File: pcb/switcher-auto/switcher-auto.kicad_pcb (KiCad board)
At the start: 4 copper layers, 234.9 x 89 mm, 120 parts, among them J1 MD-90SM, J2 Conn_02x22_Top_Bottom, J201 MD-90SM, J202 MD-90SM, J203 MD-90SM, J204 MD-90SM, J205 MD-90SM, J206 Conn_02x22_Top_Bottom, J3 Conn_02x22_Top_Bottom, J4 Conn_02x22_Top_Bottom, U1 CD74HC4067SM, U11 THS7374, U2 CD74HC4067SM, U3 CD74HC4067SM, U4 CD74HC4067SM, U5 MUX506IPWR, U6 MUX506IPWR, U7 CD74HC4067SM, U8 LM2776

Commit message: Routing checkpoint
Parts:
- removed C8: 1u, Capacitor_SMD:C_0805_2012Metric_Pad1.18x1.45mm_HandSolder
- C12: value 0.1u -> 22uF
- moved C9 1.44 mm to (58.0, 98.1), turned to 0 degrees
- moved C10 1.20 mm to (58.0, 94.9), turned to 180 degrees
- moved C13 0.33 mm to (61.6, 81.5)
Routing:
- net -5V: track 32.3 -> 59.3 mm, vias 0 -> 3
- net GND: track 33.8 -> 53.9 mm, vias 31 -> 33
- net VCC: track 43.7 -> 28.7 mm
- net /9_BVID: track 41.3 -> 39.1 mm
- net /5_BVID: track 47.1 -> 45.0 mm
- net /6_BVID: track 50.2 -> 48.2 mm
- net /7_BVID: track 53.4 -> 51.4 mm
- net /10_RAUD: track 96.4 -> 95.2 mm
- net /8_BVID: track 40.8 -> 39.6 mm
- net /11_RAUD: track 94.9 -> 94.0 mm
- net /12_RAUD: track 93.6 -> 92.8 mm
- net /6_RVID: track 64.3 -> 63.6 mm
- net /9_RVID: track 81.6 -> 81.0 mm
- net /7_RVID: track 66.7 -> 66.1 mm
- net /8_RVID: track 78.2 -> 77.6 mm
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- added copper zone on B.Cu, net GND
- added copper zone on In1.Cu, net GND
- added copper zone on In2.Cu, net VCC
- removed copper zone on In2.Cu, net GND
- removed copper zone on B.Cu, net VCC
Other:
- board text removed: "Note pin 1"

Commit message: Rev3
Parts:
- C10, C9: value 2.2uF -> 1uF
- J2: value Conn_02x22_Top_Bottom -> Inputs 0-4
- J3: value Conn_02x22_Top_Bottom -> Inputs 5-9
- J4: value Conn_02x22_Top_Bottom -> Inputs 10-14
- moved C14 0.84 mm to (66.1, 96.1), turned to -90 degrees
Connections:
- C14 pad 1: Net-(U8-C1+) -> Net-(U8-C1-)
- C14 pad 2: Net-(U8-C1-) -> Net-(U8-C1+)
- U5 pad 18: GND -> VCC
- U6 pad 18: GND -> VCC
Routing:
- net VCC: track 28.7 -> 31.8 mm, vias 12 -> 14
- net GND: track 53.9 -> 51.2 mm, vias 33 -> 31
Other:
- board text added: "${COMPANY}"
- board text added: "${TITLE} rev${REVISION}"
- board text added: "USB"

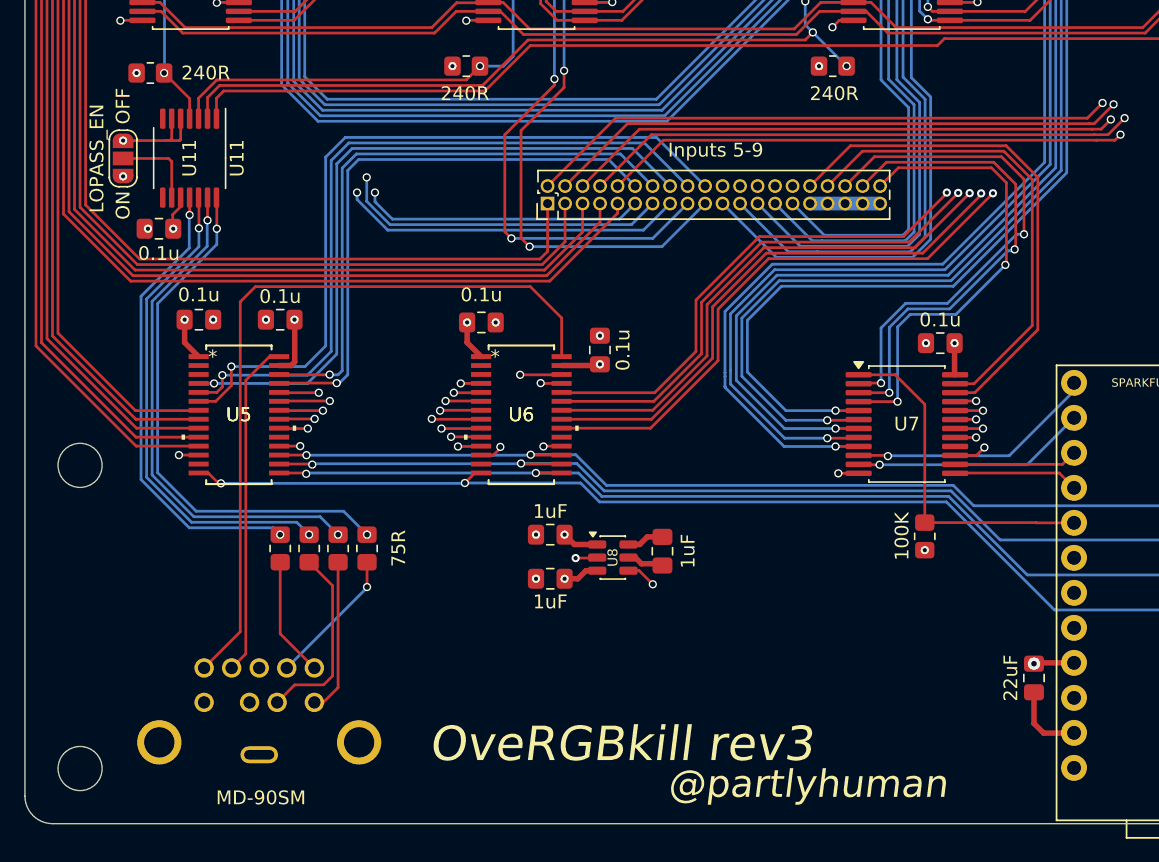
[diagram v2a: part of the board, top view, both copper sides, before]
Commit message: Switcher should run off 5V / RAW pin
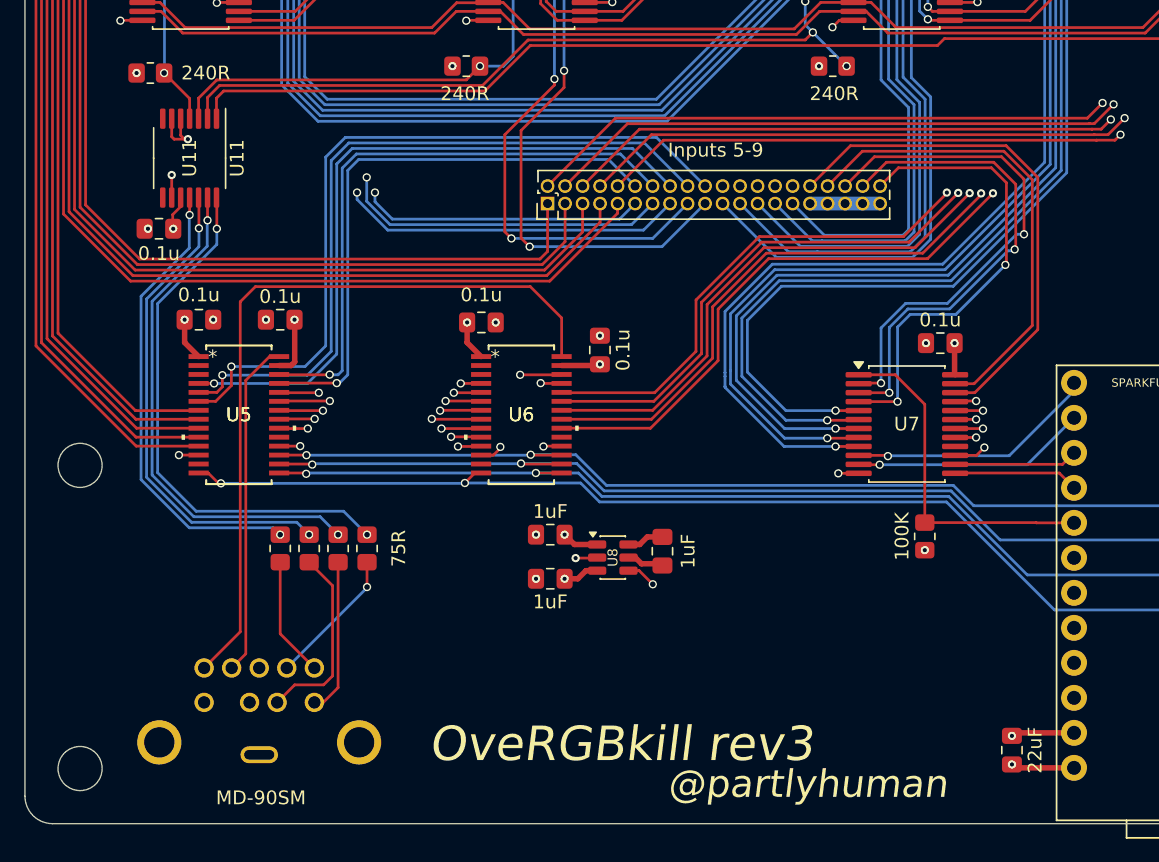
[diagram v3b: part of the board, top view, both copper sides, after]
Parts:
- removed JP11: LOPASS_EN, Jumper:SolderJumper-3_P1.3mm_Open_RoundedPad1.0x1.5mm_NumberLabels
- moved C12 5.48 mm to (91.5, 110.5), turned to 90 degrees
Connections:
- B1 pad 21: VCC -> unconnected-(B1-VCC-Pad21)
- B1 pad 24: unconnected-(B1-RAW-Pad24) -> VCC
- U11 pad 9: Net-(JP11-C) -> VCC
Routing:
- net Net-(JP11-C): track 6.23 -> 0.00 mm
- net GND: track 51.2 -> 47.1 mm, vias 31 -> 32
- net VCC: track 31.8 -> 35.1 mm

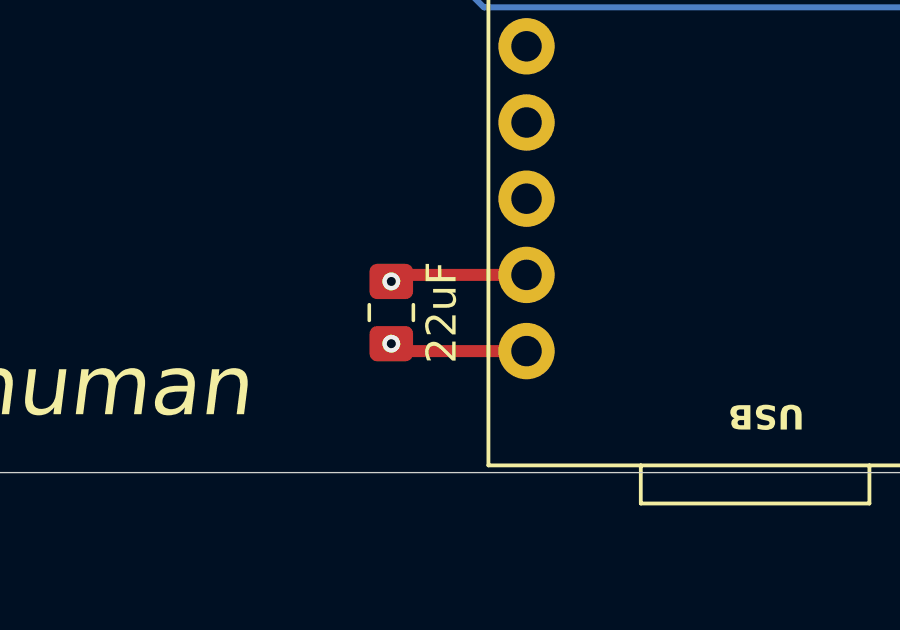
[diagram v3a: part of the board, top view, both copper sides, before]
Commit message: Fix VCC keepout
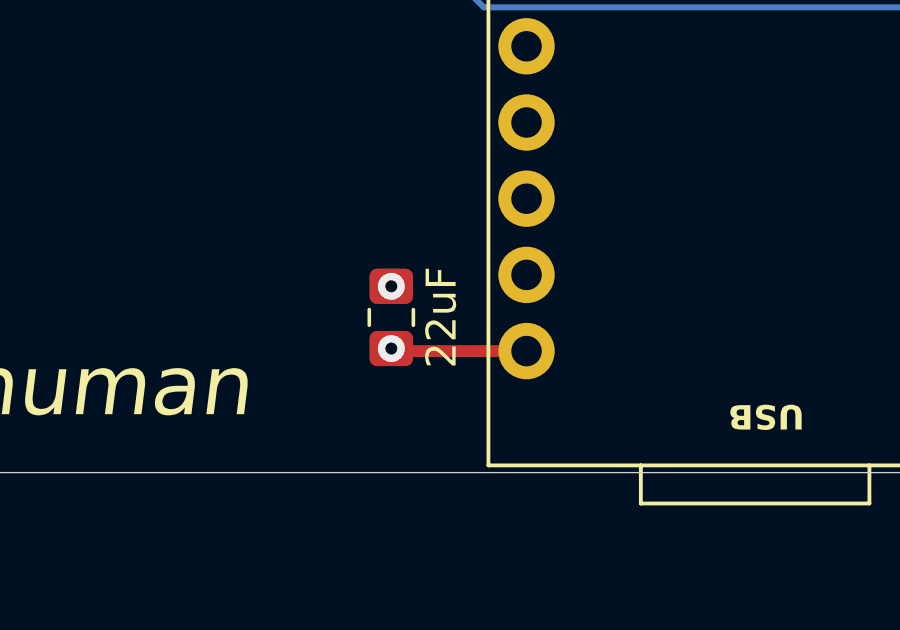
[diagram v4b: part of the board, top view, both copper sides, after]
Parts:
- moved C12 0.16 mm to (91.5, 110.7)
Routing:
- net GND: track 47.1 -> 43.0 mm
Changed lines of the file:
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@@
 	(footprint "Capacitor_SMD:C_0805_2012Metric_Pad1.18x1.45mm_HandSolder"
 		(layer "F.Cu")
-		(at 91.5 110.5375 90)
+		(at 91.5 110.7 90)
 		(descr "Capacitor SMD 0805 (2012 Metric), square (rectangular) end terminal, IPC_7351 nominal with elongated pad for handsoldering. (Body size source: IPC-SM-782 page 76, https://www.pcb-3d.com/wordpress/wp-content/uploads/ipc-sm-782a_amendment_1_and_2.pdf, https://docs.google.com/spreadsheets/d/1BsfQQcO9C6DZCsRaXUlFlo91Tg2WpOkGARC1WS5S8t0/edit?usp=sharing), generated with kicad-footprint-generator")
 		(tags "capacitor handsolder")
@@
 	)
 	(segment
+		(start 91.5 109.6625)
+		(end 91.5 109.5)
+		(width 0.4)
+		(layer "F.Cu")
+		(net 107)
+	)
+	(segment
 		(start 32.479 89.124998)
 		(end 31.050002 89.124998)
@@
 	)
 	(segment
+		(start 91.5 109.5)
+		(end 91.718004 109.281996)
+		(width 0.4)
+		(layer "F.Cu")
+		(net 107)
+	)
+	(segment
 		(start 31.7 66.2)
 		(end 31.45 66.2)
@@
 	)
 	(segment
-		(start 91.5 109.5)
-		(end 91.718004 109.281996)
-		(width 0.4)
-		(layer "F.Cu")
-		(net 107)
-	)
-	(segment
 		(start 62.475 56.275)
 		(end 62.5 56.25)
@@
 	)
 	(segment
-		(start 91.718004 109.281996)
-		(end 96.006597 109.281996)
-		(width 0.4)
-		(layer "F.Cu")
-		(net 107)
-	)
-	(segment
 		(start 87.376597 89.146996)
 		(end 88.928004 89.146996)
@@
 	)
 	(via
-		(at 91.5 109.5)
-		(size 0.6)
-		(drill 0.3)
-		(layers "F.Cu" "B.Cu")
-		(net 107)
-	)
-	(via
 		(at 31.7 66.2)
 		(size 0.6)
@@
 	)
 	(via
+		(at 91.5 109.6625)
+		(size 0.9)
+		(drill 0.4)
+		(layers "F.Cu" "B.Cu")
+		(net 107)
+	)
+	(via
 		(at 54.375 88.532756)
 		(size 0.6)
@@
 	)
 	(segment
+		(start 91.5 111.7375)
+		(end 91.6625 111.7375)
+		(width 0.4)
+		(layer "F.Cu")
+		(net 235)
+	)
+	(segment
 		(start 87.3375 48)
 		(end 87.3375 50.0875)
@@
 	)
 	(segment
+		(start 91.746996 111.821996)
+		(end 96.006597 111.821996)
+		(width 0.4)
+		(layer "F.Cu")
+		(net 235)
+	)
+	(segment
 		(start 61.2375 48)
 		(end 61.2375 49.6875)
@@
 	)
 	(segment
-		(start 91.746996 111.821996)
-		(end 96.006597 111.821996)
-		(width 0.4)
-		(layer "F.Cu")
-		(net 235)
-	)
-	(segment
 		(start 61.2375 49.6875)
 		(end 60.5 50.425)
@@
 	)
 	(segment
-		(start 91.5 111.575)
+		(start 91.6625 111.7375)
 		(end 91.746996 111.821996)
 		(width 0.4)
@@
 	)
 	(via
-		(at 91.5 111.575)
-		(size 0.6)
-		(drill 0.3)
+		(at 91.5 111.7375)
+		(size 0.9)
+		(drill 0.4)
 		(layers "F.Cu" "B.Cu")
 		(net 235)
@@
 	)
 	(zone
-		(net 0)
-		(net_name "")
-		(layer "B.Cu")
+		(net 107)
+		(net_name "GND")
+		(layers "B.Cu" "In1.Cu")
 		(hatch edge 0.5)
 		(connect_pads
-			(clearance 0)
+			(clearance 0.2)
 		)
 		(min_thickness 0.25)
 		(filled_areas_thickness no)
-		(keepout
-			(tracks allowed)
-			(vias allowed)
-			(pads allowed)
-			(copperpour not_allowed)
-			(footprints allowed)
-		)
-		(placement
-			(enabled no)
-			(sheetname "")
-		)
-		(fill
+		(fill yes
 			(thermal_gap 0.5)
 			(thermal_bridge_width 0.5)
@@
 		(polygon
 			(pts
-				(xy 94.6 110.489227) (xy 97.5 110.489227) (xy 97.5 113.189227) (xy 94.6 113.189227)
+				(xy 14.876597 14.871996) (xy 124.876597 14.871996) (xy 124.876597 124.871996) (xy 14.876597 124.871996)
 			)
 		)
 	)
 	(zone
-		(net 107)
-		(net_name "GND")
-		(layers "B.Cu" "In1.Cu")
+		(net 235)
+		(net_name "VCC")
+		(layer "In2.Cu")
 		(hatch edge 0.5)
+		(priority 2)
 		(connect_pads
-			(clearance 0.2)
+			(clearance 0.6)
 		)
 		(min_thickness 0.25)
@@
 		(polygon
 			(pts
-				(xy 14.876597 14.871996) (xy 124.876597 14.871996) (xy 124.876597 124.871996) (xy 14.876597 124.871996)
+				(xy 17.376597 24.871996) (xy 122.376597 24.871996) (xy 122.376597 119.871996) (xy 17.376597 119.871996)
 			)
 		)
 	)
 	(zone
-		(net 235)
-		(net_name "VCC")
+		(net 0)
+		(net_name "")
 		(layer "In2.Cu")
 		(hatch edge 0.5)
-		(priority 2)
 		(connect_pads
-			(clearance 0.6)
+			(clearance 0)
 		)
 		(min_thickness 0.25)
 		(filled_areas_thickness no)
-		(fill yes
+		(keepout
+			(tracks allowed)
+			(vias allowed)
+			(pads allowed)
+			(copperpour not_allowed)
+			(footprints allowed)
+		)
+		(placement
+			(enabled no)
+			(sheetname "")
+		)
+		(fill
 			(thermal_gap 0.5)
 			(thermal_bridge_width 0.5)
@@
 		(polygon
 			(pts
-				(xy 17.376597 24.871996) (xy 122.376597 24.871996) (xy 122.376597 119.871996) (xy 17.376597 119.871996)
+				(xy 94.4 110.489227) (xy 97.6 110.489227) (xy 97.6 113.3) (xy 94.4 113.3)
 			)
 		)

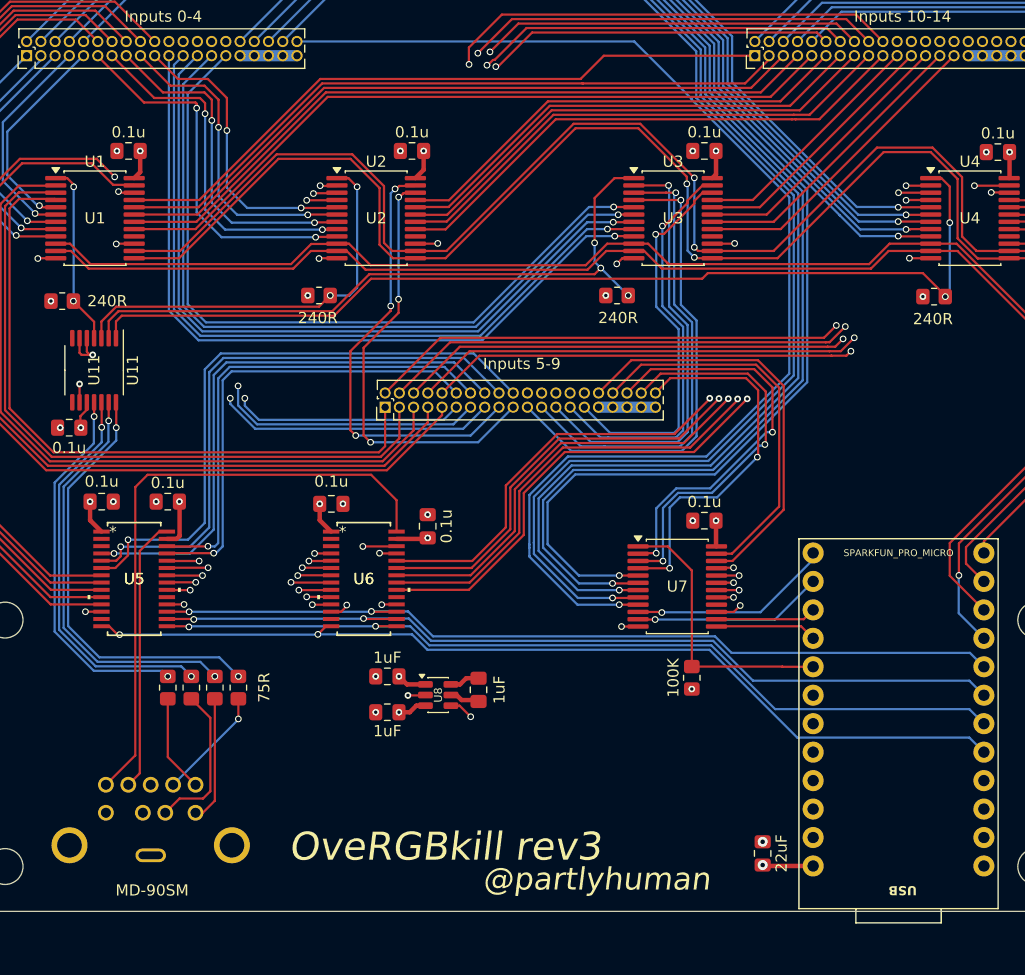
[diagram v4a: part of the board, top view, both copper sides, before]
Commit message: Add silkscreen hints for keyed connectors
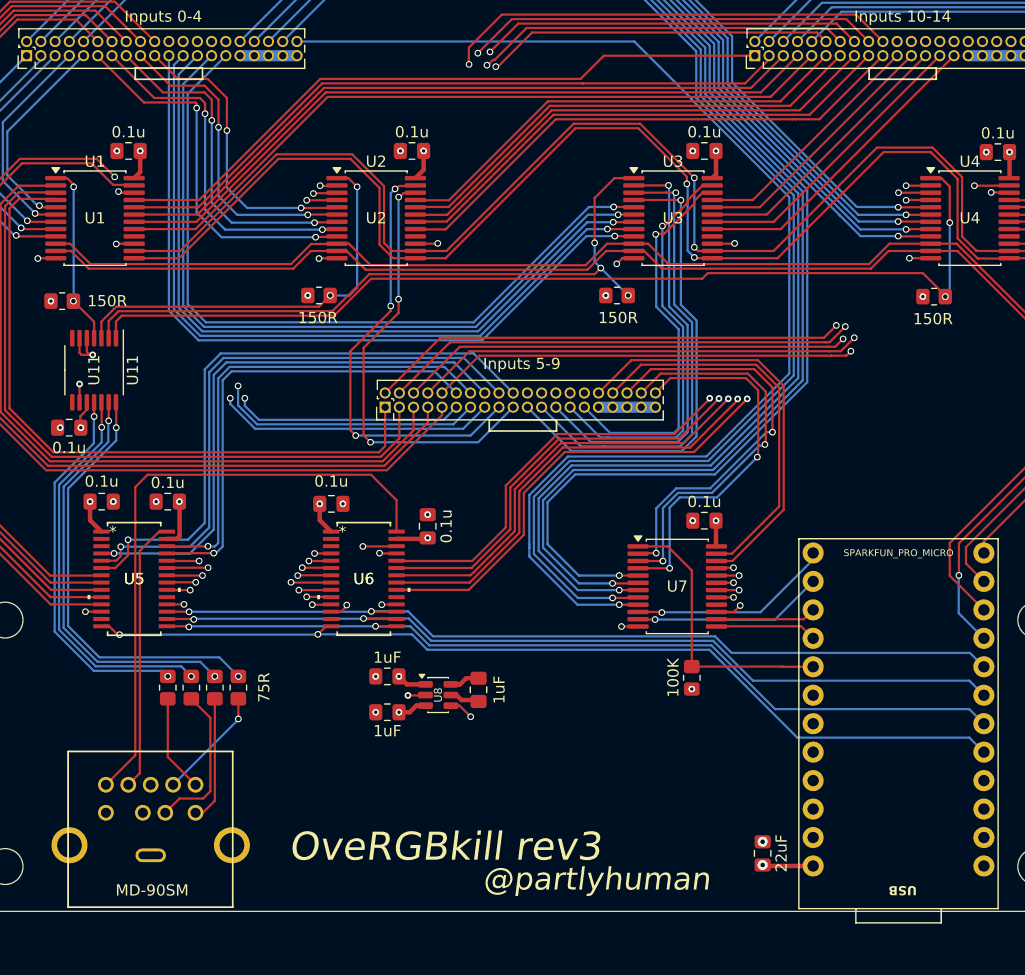
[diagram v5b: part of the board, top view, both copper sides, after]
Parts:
- R11, R12, R13, R14: value 240R -> 150R
